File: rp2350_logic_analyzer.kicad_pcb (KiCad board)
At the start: 4 copper layers, 59 x 34 mm, 35 parts, among them J1 Conn_02x04, J2 Conn_01x03, J3 Conn_01x03, J4 Conn_01x03, J5 Conn_01x03, U1 ISO7761FDBQ, U2 TLV3501AIDBV, U3 TLV3501AIDBV, U4 TLV3501AIDBV, U5 TLV3501AIDBV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

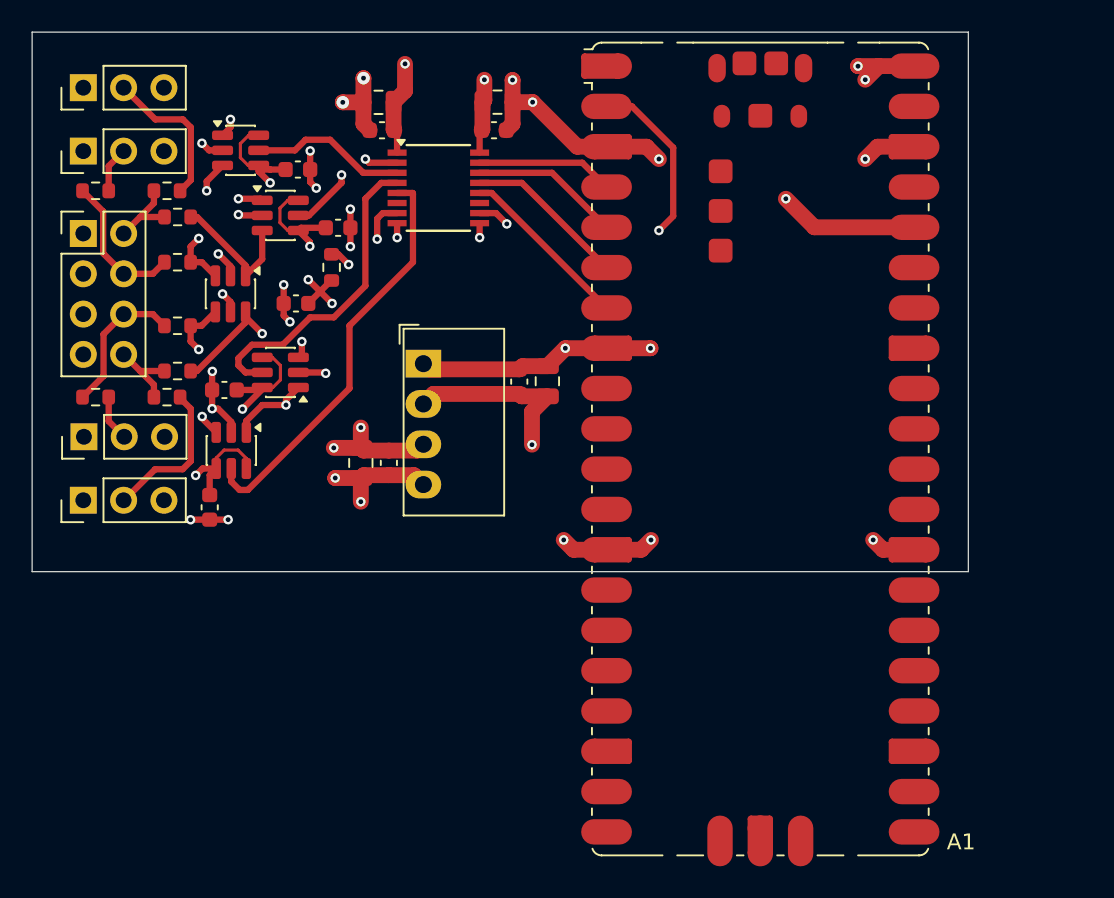
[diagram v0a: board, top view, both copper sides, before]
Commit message: Replace ISO7761FDBQ with SI8661BD-B-IS
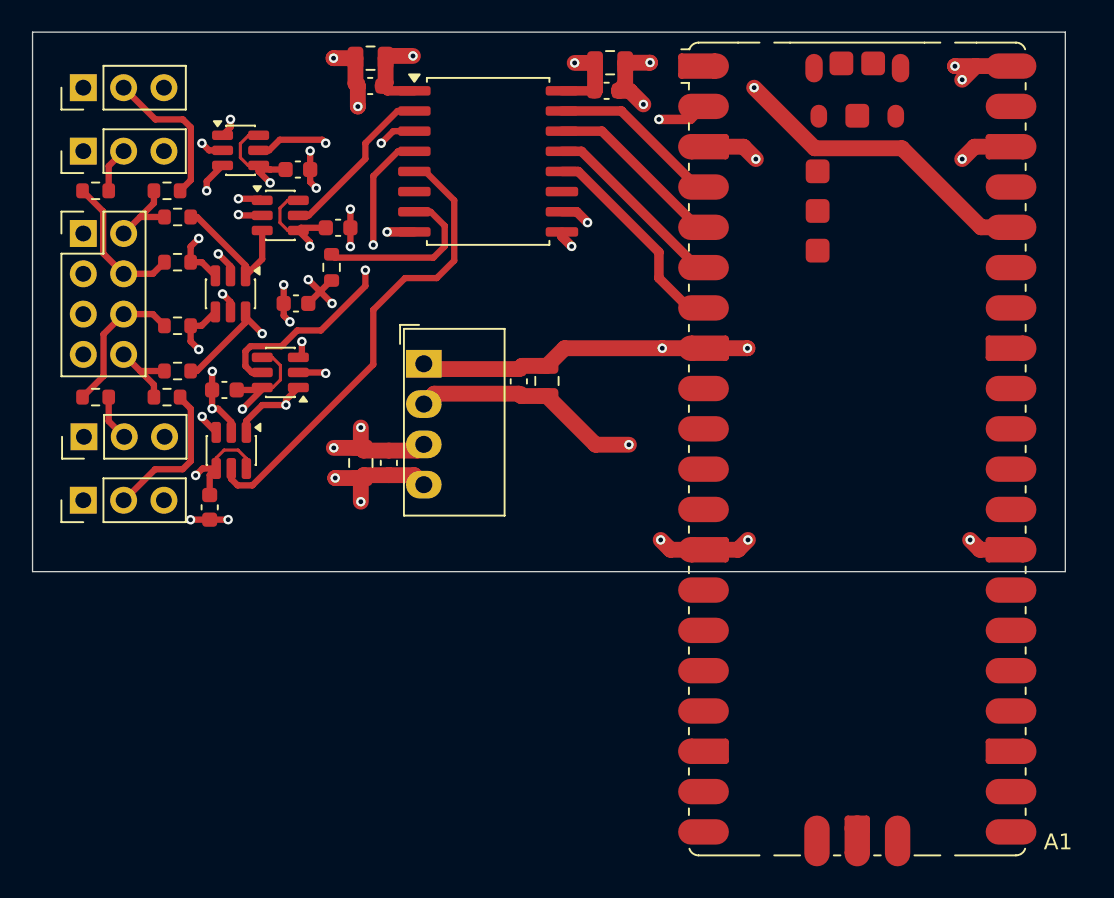
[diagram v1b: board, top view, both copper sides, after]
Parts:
- removed U1: ISO7761FDBQ, Package_SO:SSOP-16_3.9x4.9mm_P0.635mm
- added U7: Si8661BD-B-IS, Package_SO:SOIC-16W_7.5x10.3mm_P1.27mm, F.Cu at (47.2, 25.1)
- moved C7 7.52 mm to (54.7, 20.7)
- moved C13 7.52 mm to (54.9, 18.9)
- moved A1 6.11 mm to (70.5, 43.3)
- moved C6 2.89 mm to (39.8, 20.4)
- moved C12 2.83 mm to (39.8, 18.6)
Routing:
- net /PWM_SRC: track 22.6 -> 13.4 mm
- net /PWM_FROM_ISO: track 6.50 -> 11.1 mm, vias 2 -> 0
- net Net-(U7-A4): track 26.1 -> 29.8 mm
- net /+5V_USB: track 57.3 -> 60.2 mm
- net Net-(U7-A1): track 8.08 -> 10.6 mm, vias 2 -> 0
- net Net-(A1-GPIO5): track 11.0 -> 13.4 mm
- net Net-(A1-GPIO2): track 8.63 -> 10.9 mm
- net Net-(A1-GPIO3): track 9.42 -> 11.4 mm
- net Net-(U7-A3): track 19.9 -> 21.8 mm, vias 0 -> 2
- net Net-(A1-GPIO4): track 10.2 -> 12.0 mm
- net /GND: track 42.2 -> 43.5 mm
- net /+3V3: track 35.7 -> 36.9 mm
- net Net-(U7-A2): track 9.86 -> 10.5 mm, vias 0 -> 2
- net /GND_ISO: track 33.6 -> 34.2 mm
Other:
- board size 59 x 34 mm -> 65.1 x 34 mm

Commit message: Improve grounding
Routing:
- added copper zone on B.Cu, net /GND
- added copper zone on B.Cu, net /GND_ISO
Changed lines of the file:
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@@
 			(pinfunction "Pin_1")
 			(pintype "passive")
+			(zone_connect 2)
 		)
 		(pad "2" thru_hole circle
@@
 			(pinfunction "Pin_1")
 			(pintype "passive")
+			(zone_connect 2)
 		)
 		(pad "2" thru_hole circle
@@
 			(pinfunction "Pin_1")
 			(pintype "passive")
+			(zone_connect 2)
 		)
 		(pad "2" thru_hole circle
@@
 			(pinfunction "Pin_1")
 			(pintype "passive")
+			(zone_connect 2)
 		)
 		(pad "2" thru_hole circle
@@
 			(pinfunction "Pin_3")
 			(pintype "passive")
+			(zone_connect 2)
 		)
 		(pad "4" thru_hole circle
@@
 			(pinfunction "Pin_5")
 			(pintype "passive")
+			(zone_connect 2)
 		)
 		(pad "6" thru_hole circle
@@
 			(pinfunction "Pin_7")
 			(pintype "passive")
+			(zone_connect 2)
 		)
 		(pad "8" thru_hole circle
@@
 			(pinfunction "Pin_1")
 			(pintype "passive")
+			(zone_connect 2)
 		)
 		(pad "2" thru_hole circle
@@
 			(pinfunction "-Vin")
 			(pintype "power_in")
+			(zone_connect 2)
 		)
 		(pad "2" thru_hole oval
@@
 			(pinfunction "-Vout")
 			(pintype "power_out")
+			(zone_connect 2)
 		)
 		(pad "4" thru_hole oval
@@
 		(net 9)
 		(net_name "/GND")
+		(layer "B.Cu")
+		(hatch edge 0.5)
+		(priority 3)
+		(connect_pads
+			(clearance 0.25)
+		)
+		(min_thickness 0.25)
+		(filled_areas_thickness no)
+		(fill yes
+			(thermal_gap 0.5)
+			(thermal_bridge_width 0.4)
+		)
+		(polygon
+			(pts
+				(xy 51.5 17) (xy 83.614524 16.999999) (xy 83.608129 51) (xy 52.5 51) (xy 52.5 39.5) (xy 42 39.5)
+				(xy 42 35.5) (xy 51.5 35.5)
+			)
+		)
+	)
+	(zone
+		(net 44)
+		(net_name "/GND_ISO")
+		(layer "B.Cu")
+		(hatch edge 0.5)
+		(priority 2)
+		(connect_pads
+			(clearance 0.25)
+		)
+		(min_thickness 0.25)
+		(filled_areas_thickness no)
+		(fill yes
+			(thermal_gap 0.5)
+			(thermal_bridge_width 0.4)
+		)
+		(polygon
+			(pts
+				(xy 18.5 17) (xy 46 17) (xy 46 32) (xy 40.5 34.5) (xy 40.5 42) (xy 44.5 42) (xy 44.5 51) (xy 18.5 51)
+			)
+		)
+	)
+	(zone
+		(net 9)
+		(net_name "/GND")
 		(layer "In1.Cu")
 		(hatch edge 0.5)
 		(priority 1)
 		(connect_pads
-			(clearance 0.5)
+			(clearance 0.25)
 		)
-		(min_thickness 1)
+		(min_thickness 0.25)
 		(filled_areas_thickness no)
 		(fill yes
 			(thermal_gap 0.5)
-			(thermal_bridge_width 1)
+			(thermal_bridge_width 0.4)
 		)
 		(polygon
 			(pts
-				(xy 83.61 17) (xy 51.61 17) (xy 51.61 35.5) (xy 42.11 35.5) (xy 42.11 39.5) (xy 52.61 39.5) (xy 52.61 51)
+				(xy 83.61 17) (xy 51.5 17) (xy 51.5 35.5) (xy 42 35.5) (xy 42 39.5) (xy 52.5 39.5) (xy 52.5 51)
 				(xy 83.61 51)
 			)
@@
 		(hatch edge 0.5)
 		(connect_pads
-			(clearance 0.5)
+			(clearance 0.25)
 		)
-		(min_thickness 1)
+		(min_thickness 0.25)
 		(filled_areas_thickness no)
 		(fill yes
 			(thermal_gap 0.5)
-			(thermal_bridge_width 1)
+			(thermal_bridge_width 0.4)
 		)
 		(polygon

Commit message: Position newly added LDO
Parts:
- added U8: ME6203A50M3G, Package_TO_SOT_SMD:SOT-23, F.Cu at (37.3, 46.5)
- PS1: value MEE1S0505SC -> B0509S-1W
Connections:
- C10 pad 1: /+5V_ISO -> /9V_UNREG
- C9 pad 1: /+5V_ISO -> /9V_UNREG
- PS1 pad 4: /+5V_ISO -> /9V_UNREG
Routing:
- net /+5V_ISO: track 157.3 -> 147.3 mm, vias 8 -> 7
- net /9V_UNREG: track 0.00 -> 6.07 mm
- net /GND_ISO: track 34.2 -> 37.0 mm
